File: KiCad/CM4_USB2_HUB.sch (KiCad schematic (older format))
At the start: 30 parts, among them IC1 USB2517-JZX, J10 72309-8014BLF, J11 10104110-0001LF, J12 SS-52100-002, J4 72309-8014BLF, J9 Conn_02x05_Odd_Even, U3 FSUSB42MUX, Y1 24MHz

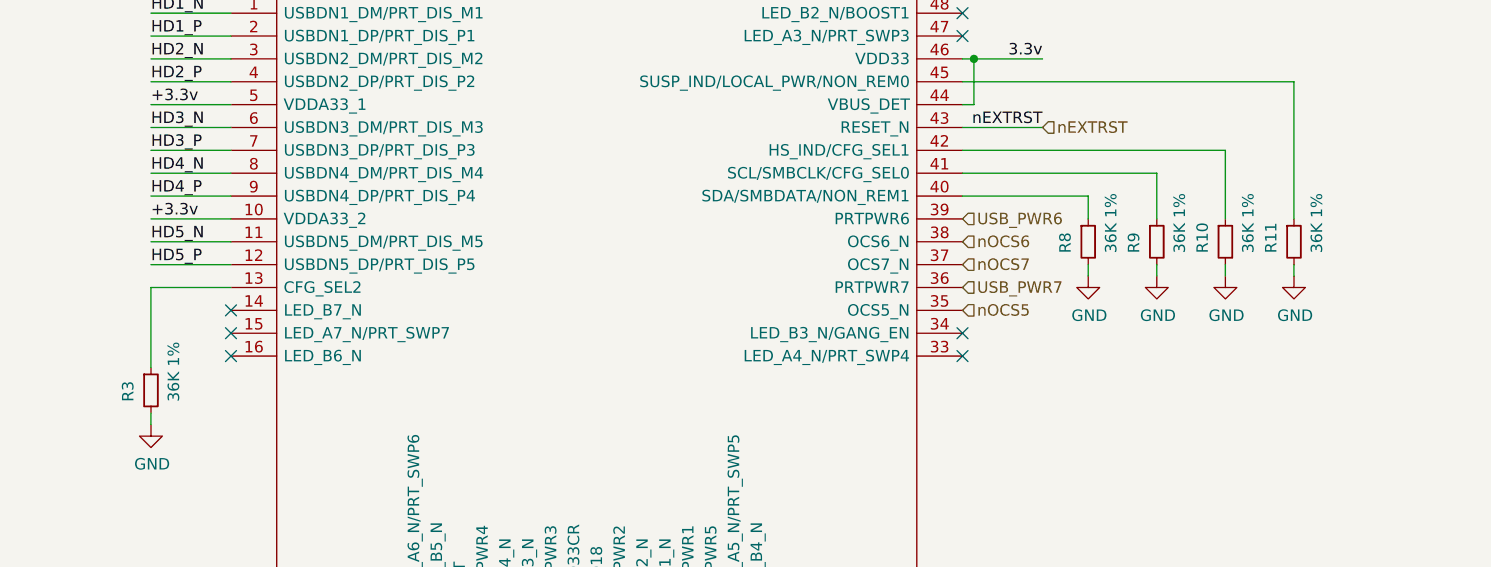
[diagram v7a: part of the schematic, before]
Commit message: More BOM detailing and small changes
Removed some NC components from the PCI-e subsection
Picked resistor footprints
Picked resistor items in the BOM
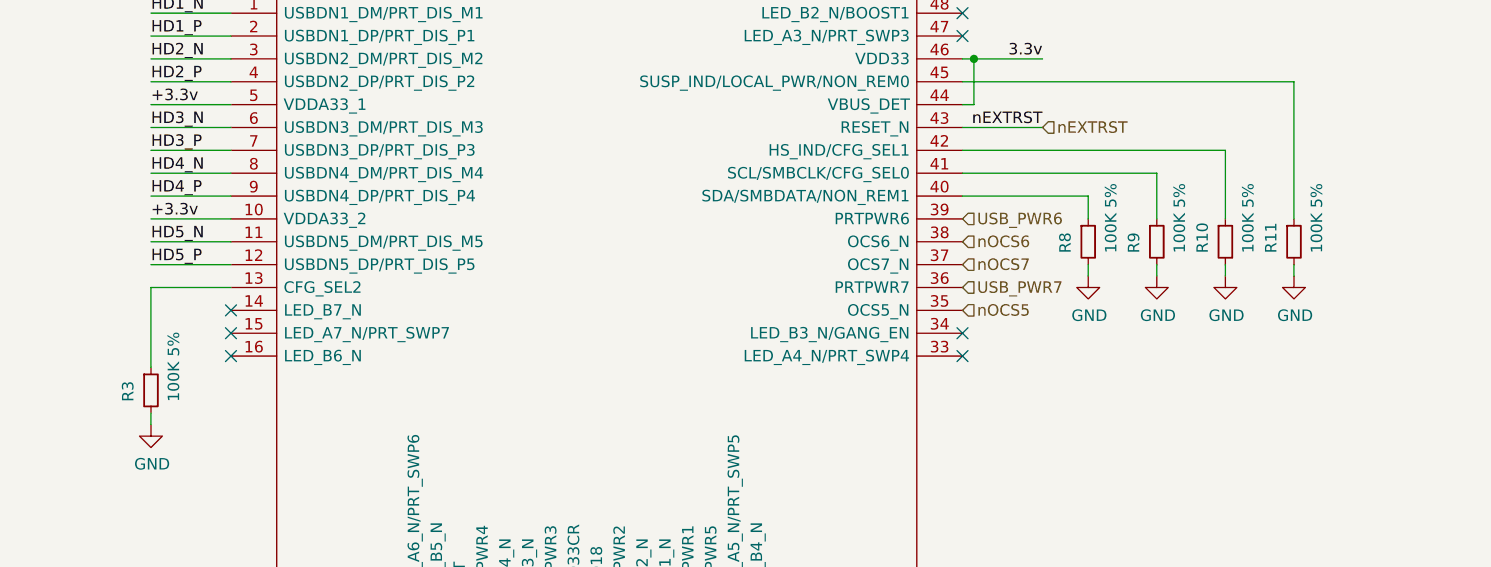
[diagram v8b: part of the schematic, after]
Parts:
- R10, R11, R3, R8, R9: value 36K 1% -> 100K 5%; footprint (none) -> CM4_MATX:R_0402_1005Metric_Pad0.72x0.64mm_HandSolder; Description (none) -> 0402 1/16W 100KOhm 5%; Mfr. (none) -> Vishay / Dale; Mfr. No (none) -> CRCW0402100KJNEDC; Mouser Part Number (none) -> 71-CRCW0402100KJNEDC; Mouser Price/Stock (none) -> https://www.mouser.co.uk/ProductDetail/Vishay-Dale/CRCW0402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
- R12, R13: Description (none) -> 0603 1/10W 2.2KOhm 1%; Mfr. (none) -> Vishay / Dale; Mfr. No (none) -> CRCW06032K20FKEAC; Mouser Part Number (none) -> 71-CRCW06032K20FKEAC; Mouser Price/Stock (none) -> https://www.mouser.co.uk/ProductDetail/Vishay-Dale/CRCW0603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
- R6: footprint (none) -> CM4_MATX:R_0603_1608Metric_Pad0.98x0.95mm_HandSolder; Description (none) -> 0603 1/16W 12KOhm 1%; Mfr. (none) -> Vishay / Dale; Mfr. No (none) -> CRCW040212K0FKED; Mouser Part Number (none) -> 71-CRCW0402-12K-E3; Mouser Price/Stock (none) -> https://www.mouser.co.uk/ProductDetail/Vishay-Dale/CRCW0402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
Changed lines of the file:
@@
 F 1 "2.2K 1%" H 7700 5950 50  0000 L CNN
 F 2 "CM4_MATX:R_0603_1608Metric_Pad0.98x0.95mm_HandSolder" H 8050 6000 50  0001 C CNN
-F 3 "~" H 8050 6000 50  0001 C CNN
+F 3 "https://www.mouser.co.uk/datasheet/2/427/crcwce3-1762584.pdf" H 8050 6000 50  0001 C CNN
+F 4 "0603 1/10W 2.2KOhm 1%" H 8050 6000 50  0001 C CNN "Description"
+F 5 "Vishay / Dale" H 8050 6000 50  0001 C CNN "Mfr."
+F 6 "CRCW06032K20FKEAC" H 8050 6000 50  0001 C CNN "Mfr. No"
+F 7 "71-CRCW06032K20FKEAC" H 8050 6000 50  0001 C CNN "Mouser Part Number"
+F 8 "https://www.mouser.co.uk/ProductDetail/Vishay-Dale/CRCW06032K20FKEAC/?qs=sGAEpiMZZMvdGkrng054t0DrEhLhGh8gE5m%2FjtqQkMzhxZ01md9MxQ%3D%3D" H 8050 6000 50  0001 C CNN "Mouser Price/Stock"
 	1    8050 6000
 	1    0    0    -1
@@
 P 5400 4400
 F 0 "R8" V 5300 4350 50  0000 L CNN
-F 1 "36K 1%" V 5500 4350 50  0000 L CNN
-F 2 "" H 5400 4400 50  0001 C CNN
-F 3 "~" H 5400 4400 50  0001 C CNN
+F 1 "100K 5%" V 5500 4350 50  0000 L CNN
+F 2 "CM4_MATX:R_0402_1005Metric_Pad0.72x0.64mm_HandSolder" H 5400 4400 50  0001 C CNN
+F 3 "https://www.mouser.co.uk/datasheet/2/427/crcwce3-1762584.pdf" H 5400 4400 50  0001 C CNN
+F 4 "0402 1/16W 100KOhm 5%" H 5400 4400 50  0001 C CNN "Description"
+F 5 "Vishay / Dale" H 5400 4400 50  0001 C CNN "Mfr."
+F 6 "CRCW0402100KJNEDC" H 5400 4400 50  0001 C CNN "Mfr. No"
+F 7 "71-CRCW0402100KJNEDC" H 5400 4400 50  0001 C CNN "Mouser Part Number"
+F 8 "https://www.mouser.co.uk/ProductDetail/Vishay-Dale/CRCW0402100KJNEDC/?qs=sGAEpiMZZMvdGkrng054t8r8AhKhXLMmPUoOyY5yMhyGmvgn6AkAGw%3D%3D" H 5400 4400 50  0001 C CNN "Mouser Price/Stock"
 	1    5400 4400
 	1    0    0    -1
@@
 P 5700 4400
 F 0 "R9" V 5600 4350 50  0000 L CNN
-F 1 "36K 1%" V 5800 4350 50  0000 L CNN
-F 2 "" H 5700 4400 50  0001 C CNN
-F 3 "~" H 5700 4400 50  0001 C CNN
+F 1 "100K 5%" V 5800 4350 50  0000 L CNN
+F 2 "CM4_MATX:R_0402_1005Metric_Pad0.72x0.64mm_HandSolder" H 5700 4400 50  0001 C CNN
+F 3 "https://www.mouser.co.uk/datasheet/2/427/crcwce3-1762584.pdf" H 5700 4400 50  0001 C CNN
+F 4 "0402 1/16W 100KOhm 5%" H 5700 4400 50  0001 C CNN "Description"
+F 5 "Vishay / Dale" H 5700 4400 50  0001 C CNN "Mfr."
+F 6 "CRCW0402100KJNEDC" H 5700 4400 50  0001 C CNN "Mfr. No"
+F 7 "71-CRCW0402100KJNEDC" H 5700 4400 50  0001 C CNN "Mouser Part Number"
+F 8 "https://www.mouser.co.uk/ProductDetail/Vishay-Dale/CRCW0402100KJNEDC/?qs=sGAEpiMZZMvdGkrng054t8r8AhKhXLMmPUoOyY5yMhyGmvgn6AkAGw%3D%3D" H 5700 4400 50  0001 C CNN "Mouser Price/Stock"
 	1    5700 4400
 	1    0    0    -1
@@
 P 6000 4400
 F 0 "R10" V 5900 4350 50  0000 L CNN
-F 1 "36K 1%" V 6100 4350 50  0000 L CNN
-F 2 "" H 6000 4400 50  0001 C CNN
-F 3 "~" H 6000 4400 50  0001 C CNN
+F 1 "100K 5%" V 6100 4350 50  0000 L CNN
+F 2 "CM4_MATX:R_0402_1005Metric_Pad0.72x0.64mm_HandSolder" H 6000 4400 50  0001 C CNN
+F 3 "https://www.mouser.co.uk/datasheet/2/427/crcwce3-1762584.pdf" H 6000 4400 50  0001 C CNN
+F 4 "0402 1/16W 100KOhm 5%" H 6000 4400 50  0001 C CNN "Description"
+F 5 "Vishay / Dale" H 6000 4400 50  0001 C CNN "Mfr."
+F 6 "CRCW0402100KJNEDC" H 6000 4400 50  0001 C CNN "Mfr. No"
+F 7 "71-CRCW0402100KJNEDC" H 6000 4400 50  0001 C CNN "Mouser Part Number"
+F 8 "https://www.mouser.co.uk/ProductDetail/Vishay-Dale/CRCW0402100KJNEDC/?qs=sGAEpiMZZMvdGkrng054t8r8AhKhXLMmPUoOyY5yMhyGmvgn6AkAGw%3D%3D" H 6000 4400 50  0001 C CNN "Mouser Price/Stock"
 	1    6000 4400
 	1    0    0    -1
@@
 P 6300 4400
 F 0 "R11" V 6200 4350 50  0000 L CNN
-F 1 "36K 1%" V 6400 4350 50  0000 L CNN
-F 2 "" H 6300 4400 50  0001 C CNN
-F 3 "~" H 6300 4400 50  0001 C CNN
+F 1 "100K 5%" V 6400 4350 50  0000 L CNN
+F 2 "CM4_MATX:R_0402_1005Metric_Pad0.72x0.64mm_HandSolder" H 6300 4400 50  0001 C CNN
+F 3 "https://www.mouser.co.uk/datasheet/2/427/crcwce3-1762584.pdf" H 6300 4400 50  0001 C CNN
+F 4 "0402 1/16W 100KOhm 5%" H 6300 4400 50  0001 C CNN "Description"
+F 5 "Vishay / Dale" H 6300 4400 50  0001 C CNN "Mfr."
+F 6 "CRCW0402100KJNEDC" H 6300 4400 50  0001 C CNN "Mfr. No"
+F 7 "71-CRCW0402100KJNEDC" H 6300 4400 50  0001 C CNN "Mouser Part Number"
+F 8 "https://www.mouser.co.uk/ProductDetail/Vishay-Dale/CRCW0402100KJNEDC/?qs=sGAEpiMZZMvdGkrng054t8r8AhKhXLMmPUoOyY5yMhyGmvgn6AkAGw%3D%3D" H 6300 4400 50  0001 C CNN "Mouser Price/Stock"
 	1    6300 4400
 	1    0    0    -1
@@
 F 0 "R6" V 2754 1200 50  0000 C CNN
 F 1 "12K 1%" V 2845 1200 50  0000 C CNN
-F 2 "" H 2950 1200 50  0001 C CNN
-F 3 "~" H 2950 1200 50  0001 C CNN
+F 2 "CM4_MATX:R_0603_1608Metric_Pad0.98x0.95mm_HandSolder" H 2950 1200 50  0001 C CNN
+F 3 "https://www.mouser.co.uk/datasheet/2/427/dcrcwe3-1762152.pdf" H 2950 1200 50  0001 C CNN
+F 4 "0603 1/16W 12KOhm 1%" H 2950 1200 50  0001 C CNN "Description"
+F 5 "Vishay / Dale" H 2950 1200 50  0001 C CNN "Mfr."
+F 6 "CRCW040212K0FKED" H 2950 1200 50  0001 C CNN "Mfr. No"
+F 7 "71-CRCW0402-12K-E3" H 2950 1200 50  0001 C CNN "Mouser Part Number"
+F 8 "https://www.mouser.co.uk/ProductDetail/Vishay-Dale/CRCW040212K0FKED/?qs=sGAEpiMZZMvdGkrng054txEw7b1YnvGuGxPcVgtIGNs%3D" H 2950 1200 50  0001 C CNN "Mouser Price/Stock"
 	1    2950 1200
 	0    1    1    0
@@
 P 1300 5050
 F 0 "R3" V 1200 5000 50  0000 L CNN
-F 1 "36K 1%" V 1400 5000 50  0000 L CNN
-F 2 "" H 1300 5050 50  0001 C CNN
-F 3 "~" H 1300 5050 50  0001 C CNN
+F 1 "100K 5%" V 1400 5000 50  0000 L CNN
+F 2 "CM4_MATX:R_0402_1005Metric_Pad0.72x0.64mm_HandSolder" H 1300 5050 50  0001 C CNN
+F 3 "https://www.mouser.co.uk/datasheet/2/427/crcwce3-1762584.pdf" H 1300 5050 50  0001 C CNN
+F 4 "0402 1/16W 100KOhm 5%" H 1300 5050 50  0001 C CNN "Description"
+F 5 "Vishay / Dale" H 1300 5050 50  0001 C CNN "Mfr."
+F 6 "CRCW0402100KJNEDC" H 1300 5050 50  0001 C CNN "Mfr. No"
+F 7 "71-CRCW0402100KJNEDC" H 1300 5050 50  0001 C CNN "Mouser Part Number"
+F 8 "https://www.mouser.co.uk/ProductDetail/Vishay-Dale/CRCW0402100KJNEDC/?qs=sGAEpiMZZMvdGkrng054t8r8AhKhXLMmPUoOyY5yMhyGmvgn6AkAGw%3D%3D" H 1300 5050 50  0001 C CNN "Mouser Price/Stock"
 	1    1300 5050
 	1    0    0    -1
@@
 F 1 "2.2K 1%" H 7800 5150 50  0000 L CNN
 F 2 "CM4_MATX:R_0603_1608Metric_Pad0.98x0.95mm_HandSolder" H 8150 5200 50  0001 C CNN
-F 3 "~" H 8150 5200 50  0001 C CNN
+F 3 "https://www.mouser.co.uk/datasheet/2/427/crcwce3-1762584.pdf" H 8150 5200 50  0001 C CNN
+F 4 "0603 1/10W 2.2KOhm 1%" H 8150 5200 50  0001 C CNN "Description"
+F 5 "Vishay / Dale" H 8150 5200 50  0001 C CNN "Mfr."
+F 6 "CRCW06032K20FKEAC" H 8150 5200 50  0001 C CNN "Mfr. No"
+F 7 "71-CRCW06032K20FKEAC" H 8150 5200 50  0001 C CNN "Mouser Part Number"
+F 8 "https://www.mouser.co.uk/ProductDetail/Vishay-Dale/CRCW06032K20FKEAC/?qs=sGAEpiMZZMvdGkrng054t0DrEhLhGh8gE5m%2FjtqQkMzhxZ01md9MxQ%3D%3D" H 8150 5200 50  0001 C CNN "Mouser Price/Stock"
 	1    8150 5200
 	1    0    0    -1
